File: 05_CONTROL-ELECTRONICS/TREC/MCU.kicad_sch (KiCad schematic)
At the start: 9 parts, among them U1 STM32F401RETx

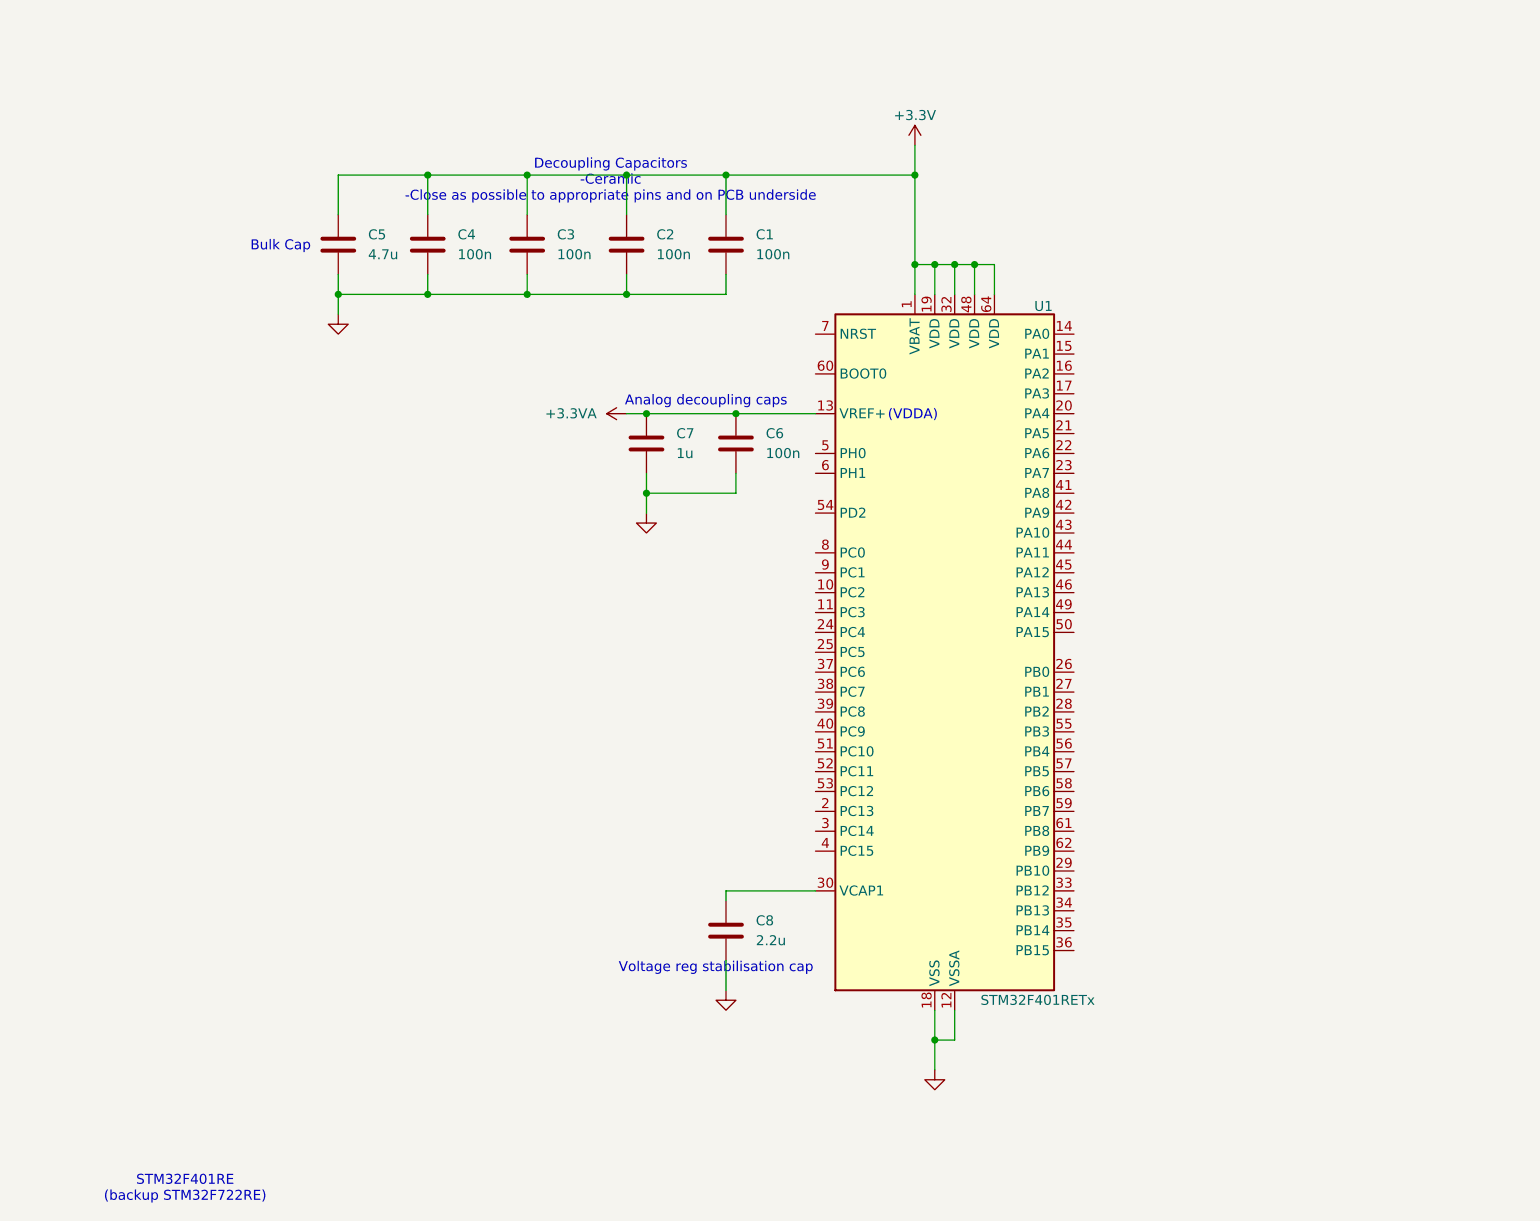
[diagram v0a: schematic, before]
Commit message: Added clock, serial, and USB to TREC MCU schematic
Included 16MHz external clock, USB B Micro connector, and 4-pin male connector for serial access to MCU pins on schematic.
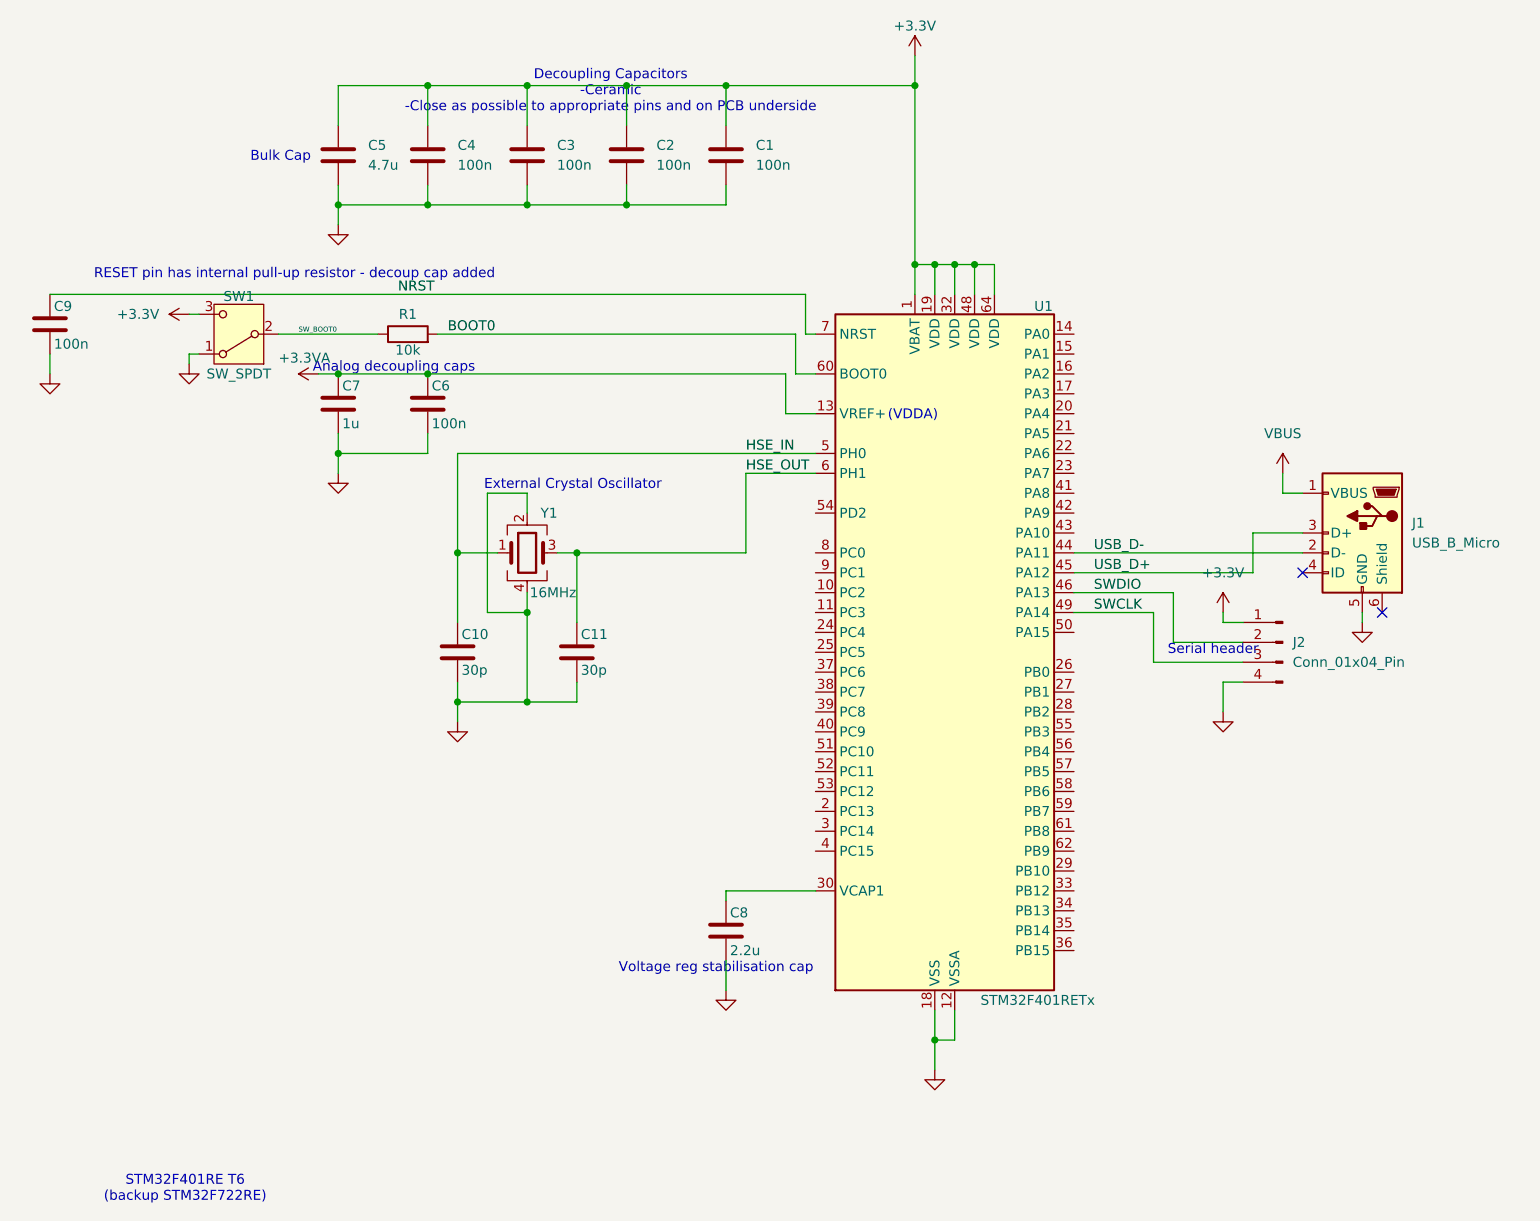
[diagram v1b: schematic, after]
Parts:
- added C10, C11: 30p, symbol Device:C
- added C9: 100n, symbol Device:C
- added J1: USB_B_Micro, symbol Connector:USB_B_Micro
- added J2: Conn_01x04_Pin, symbol Connector:Conn_01x04_Pin
- added R1: 10k, symbol Device:R
- added SW1: SW_SPDT, symbol Switch:SW_SPDT
- added Y1: 16MHz, symbol Device:Crystal_GND24
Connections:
- net +3.3V: now also J2.1 (Pin_1), SW1.3 (C)
- net GND: now also C10.2, C11.2, C9.2, J1.5 (GND), J2.4 (Pin_4), SW1.1 (A), Y1.2, Y1.4
- net USB_D-: now reaches U1.44 (PA11)
- net USB_D-: now also J1.2 (D-)
- net USB_D+: now reaches U1.45 (PA12)
- net USB_D+: now also J1.3 (D+)
- net SWDIO: now reaches U1.46 (PA13)
- net SWDIO: now also J2.2 (Pin_2)
- net SWCLK: now reaches U1.49 (PA14)
- net SWCLK: now also J2.3 (Pin_3)
- net HSE_IN: now reaches U1.5 (PH0)
- net HSE_IN: now also C10.1, Y1.1
- net HSE_OUT: now reaches U1.6 (PH1)
- net HSE_OUT: now also C11.1, Y1.3
- net BOOT0: now reaches U1.60 (BOOT0)
- net BOOT0: now also R1.2
- net NRST: now reaches U1.7 (NRST)
- net NRST: now also C9.1
- new net SW_BOOT0: R1.1, SW1.2 (B)
- new net VBUS: J1.1 (VBUS)
- no-connect marks 0 -> 2
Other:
- note added: "External Crystal Oscillator"
- note added: "RESET pin has internal pull-up resistor - decoup cap added"
- note added: "STM32F401RE T6 (backup STM32F722RE)"
- note added: "Serial header"
- note removed: "STM32F401RE (backup STM32F722RE)"
- moved on the sheet: C1, C2, C3, C4, C5, C6, C7
